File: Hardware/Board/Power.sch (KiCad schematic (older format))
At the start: 76 parts, among them Q1 Q_NMOS_DGS, Q2 Q_NMOS_DGS, Q3 Q_NMOS_DGS, Q4 Q_NMOS_DGS, U10 MAX17572, U11 MAX17572, U12 MAX17574, U8 MAX17572, U9 MAX17572

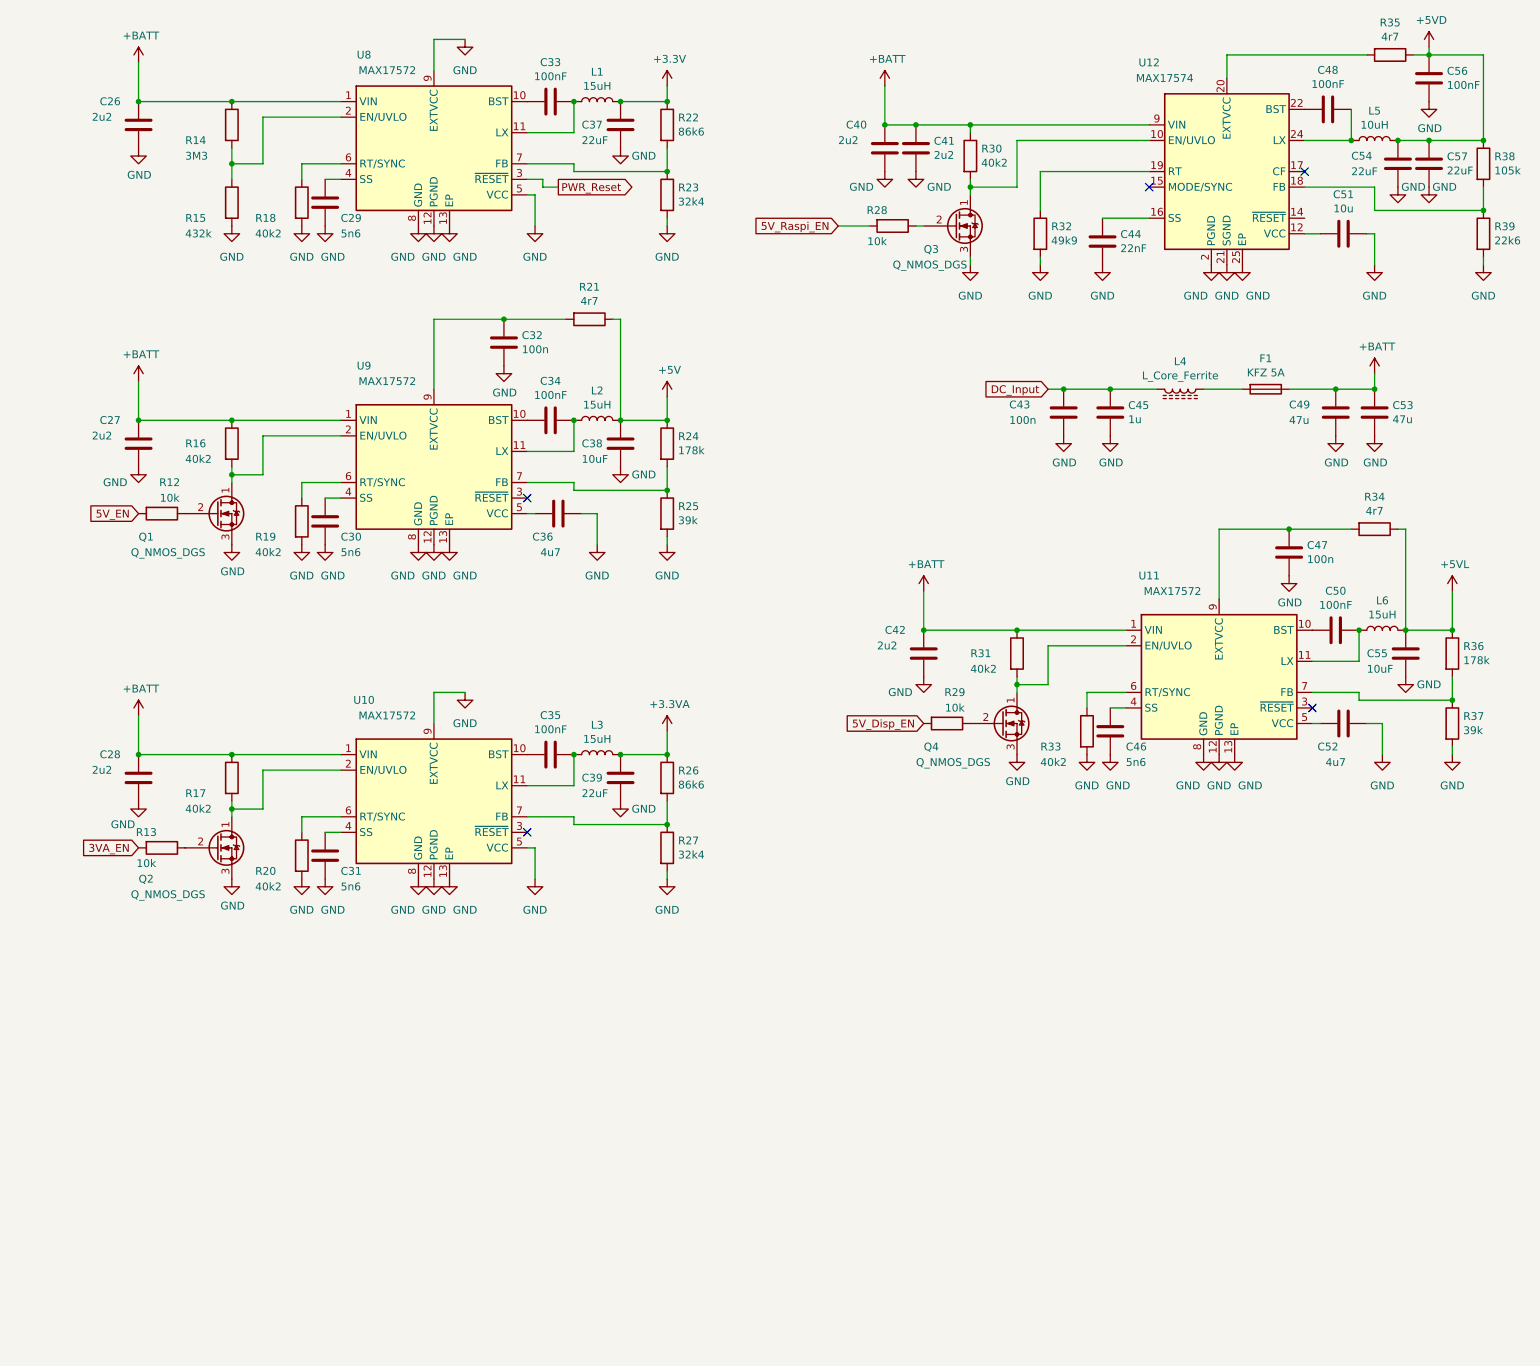
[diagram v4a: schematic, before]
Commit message: Octo SPI Flash und RAM zugefügt, weitere Bezeichnungen auf Stand gebracht
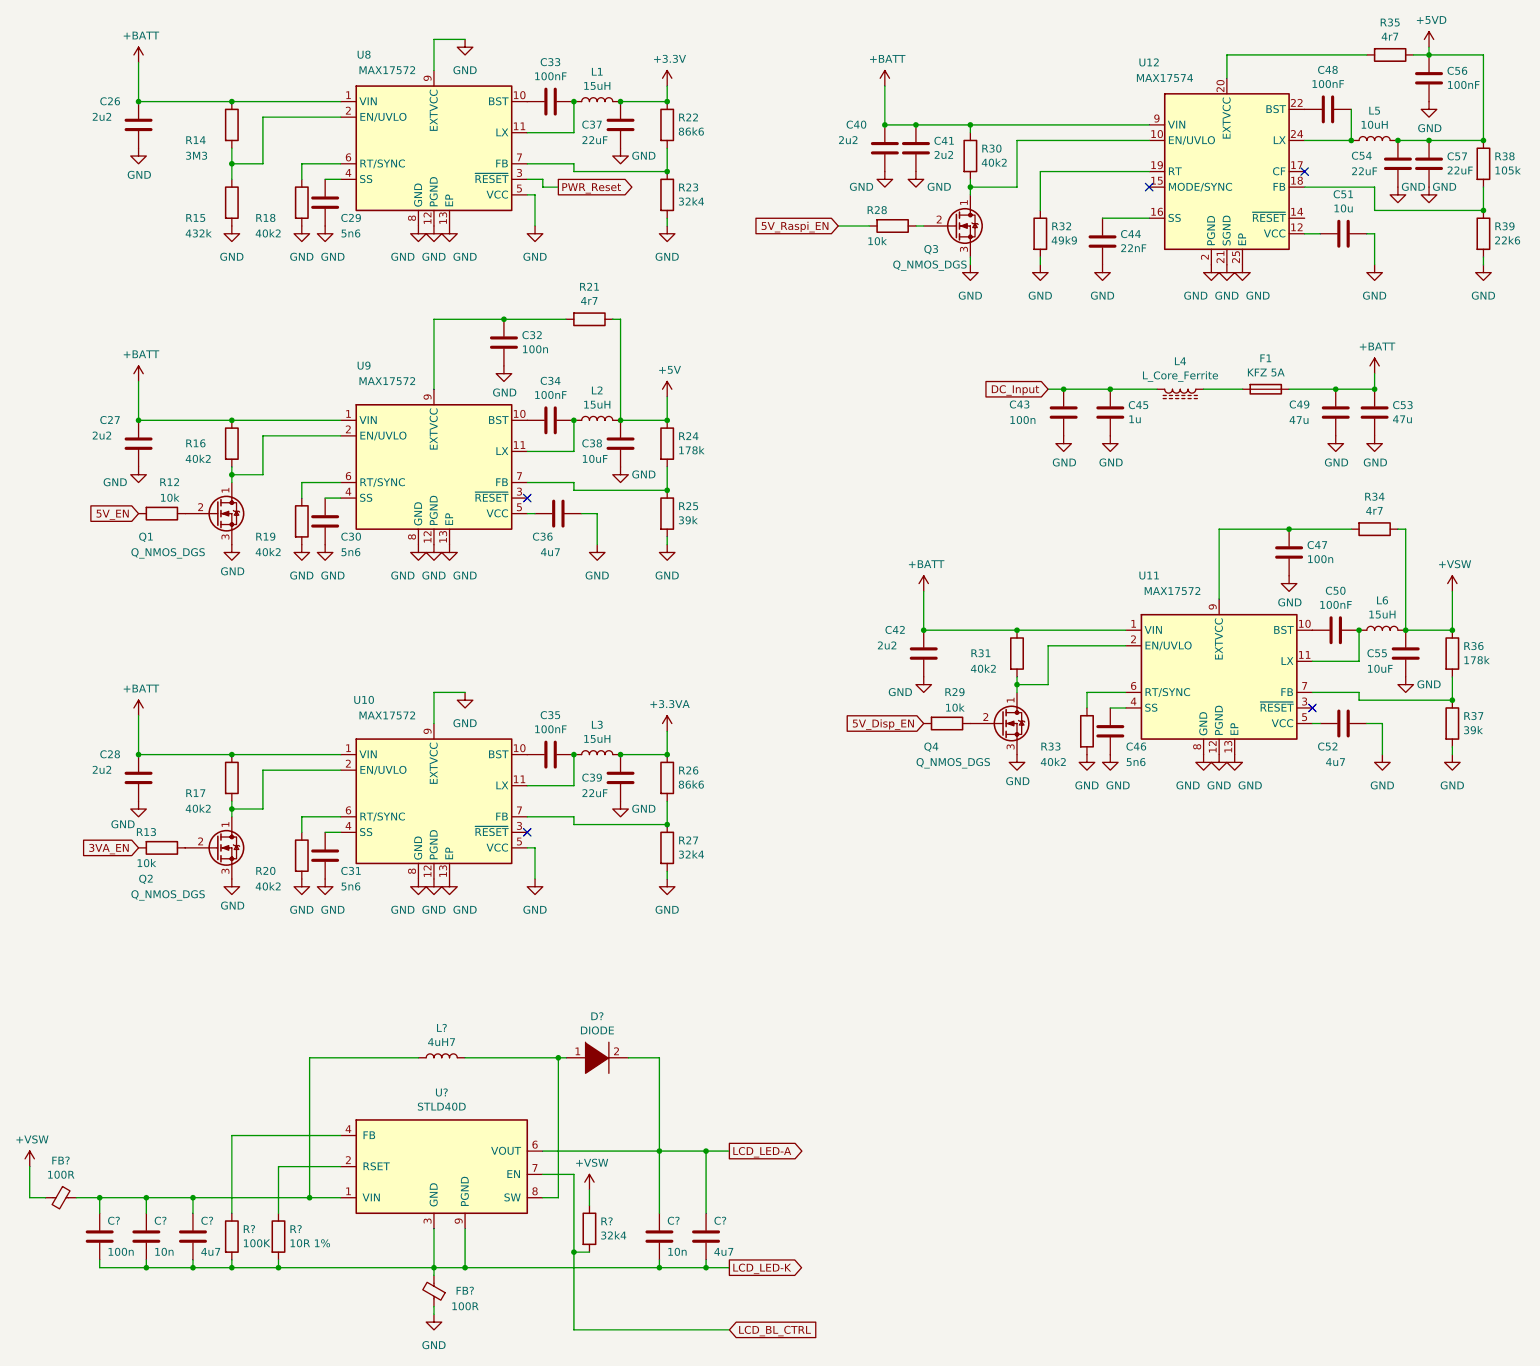
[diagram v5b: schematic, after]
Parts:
- added C? (x2): 4u7, Capacitor_SMD:C_0603_1608Metric, symbol Device:C
- added C? (x2): 10n, Capacitor_SMD:C_0603_1608Metric, symbol Device:C
- added C?: 100n, Capacitor_SMD:C_0603_1608Metric, symbol Device:C
- added D?: DIODE, symbol pspice:DIODE
- added FB? (x2): 100R, Inductor_SMD:L_0603_1608Metric, symbol Device:Ferrite_Bead_Small
- added L?: 4uH7, symbol Device:L
- added R?: 10R 1%, Resistor_SMD:R_0603_1608Metric, symbol Device:R
- added R?: 100K, Resistor_SMD:R_0603_1608Metric, symbol Device:R
- added R?: 32k4, Resistor_SMD:R_0603_1608Metric, symbol Device:R
- added U?: STLD40D, symbol DC_DC_Wandler:STLD40D
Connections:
- net GND: now also FB?.1
- net +5VL renamed +VSW
- net +VSW: now also FB?.2, R?.1
- new net: C?.1, C?.1, C?.1, FB?.1, L?.1, U?.1 (VIN)
- new net: R?.1, U?.2 (RSET)
- new net: R?.1, U?.4 (FB)
- new net: D?.1 (K), L?.2, U?.8 (SW)
- new net LCD_BL_CTRL: R?.2, U?.7 (EN)
- new net LCD_LED-A: C?.1, C?.1, D?.2 (A), U?.6 (VOUT)
- new net LCD_LED-K: C?.2, C?.2, C?.2, C?.2, C?.2, FB?.2, R?.2, R?.2, U?.3 (GND), U?.9 (PGND)

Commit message: Eine Menge Arbeit auf der GPN, fast fertig im Schaltplan.
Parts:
- removed Q4: Q_NMOS_DGS, symbol Device:Q_NMOS_DGS
- added Q?: Q_NMOS_DGS, symbol Device:Q_NMOS_DGS
- U?: symbol DC_DC_Wandler:STLD40D -> Womo-rescue:STLD40D-DC_DC_Wandler
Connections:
- net GND: now also Q?.3 (S)
- net at R31.2, U11.2 (EN/UVLO): now also Q?.1 (D)
- net at R29.1: now also Q?.2 (G)
- net 5V_Disp_EN renamed VSW_Disp_EN

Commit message: Board to Board Verbindung eingefügt
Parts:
- gave numbers to parts that had none: 14
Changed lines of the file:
@@
 EESchema Schematic File Version 4
 LIBS:Womo-cache
-EELAYER 29 0
+EELAYER 26 0
 EELAYER END
 $Descr A3 16535 11693
@@
 	10150 4750 10150 5000
 $Comp
-L Womo-rescue:STLD40D-DC_DC_Wandler U?
+L Womo-rescue:STLD40D-DC_DC_Wandler U16
 U 1 1 5DD49EC0
 P 3650 8050
-AR Path="/5C8BBC9A/5DD49EC0" Ref="U?"  Part="1"
+AR Path="/5C8BBC9A/5DD49EC0" Ref="U16"  Part="1"
 AR Path="/5E0C5EEA/5DD49EC0" Ref="U?"  Part="1"
-F 0 "U?" H 3650 8125 50  0000 C CNN
+F 0 "U16" H 3650 8125 50  0000 C CNN
 F 1 "STLD40D" H 3650 8034 50  0000 C CNN
 F 2 "" H 3650 8050 50  0001 C CNN
@@
 $EndComp
 $Comp
-L power:GND #PWR?
+L power:GND #PWR0228
 U 1 1 5DD5B9F7
 P 3600 9400
-AR Path="/5C8BBC9A/5DD5B9F7" Ref="#PWR?"  Part="1"
+AR Path="/5C8BBC9A/5DD5B9F7" Ref="#PWR0228"  Part="1"
 AR Path="/5E0C5EEA/5DD5B9F7" Ref="#PWR?"  Part="1"
-F 0 "#PWR?" H 3600 9150 50  0001 C CNN
+F 0 "#PWR0228" H 3600 9150 50  0001 C CNN
 F 1 "GND" H 3600 9200 50  0000 C CNN
 F 2 "" H 3600 9400 50  0001 C CNN
@@
 	2300 8250 2300 8750
 $Comp
-L Device:L L?
+L Device:L L7
 U 1 1 5DD8E83C
 P 3650 7750
-AR Path="/5C8BBC9A/5DD8E83C" Ref="L?"  Part="1"
+AR Path="/5C8BBC9A/5DD8E83C" Ref="L7"  Part="1"
 AR Path="/5E0C5EEA/5DD8E83C" Ref="L?"  Part="1"
-F 0 "L?" V 3840 7750 50  0000 C CNN
+F 0 "L7" V 3840 7750 50  0000 C CNN
 F 1 "4uH7" V 3749 7750 50  0000 C CNN
 F 2 "" H 3650 7750 50  0001 C CNN
@@
 P 1200 8650
 AR Path="/5C8BBC97/5DD99356" Ref="FB?"  Part="1"
-AR Path="/5C8BBC9A/5DD99356" Ref="FB?"  Part="1"
+AR Path="/5C8BBC9A/5DD99356" Ref="FB16"  Part="1"
 AR Path="/5E0C5EEA/5DD99356" Ref="FB?"  Part="1"
-F 0 "FB?" V 963 8650 50  0000 C CNN
+F 0 "FB16" V 963 8650 50  0000 C CNN
 F 1 "100R" V 1054 8650 50  0000 C CNN
 F 2 "Inductor_SMD:L_0603_1608Metric" V 1130 8650 50  0001 C CNN
@@
 $EndComp
 $Comp
-L Device:C C?
+L Device:C C69
 U 1 1 5DDA036C
 P 5350 8900
-AR Path="/5C8BBC9A/5DDA036C" Ref="C?"  Part="1"
+AR Path="/5C8BBC9A/5DDA036C" Ref="C69"  Part="1"
 AR Path="/5E0C5EEA/5DDA036C" Ref="C?"  Part="1"
-F 0 "C?" H 5400 9000 50  0000 L CNN
+F 0 "C69" H 5400 9000 50  0000 L CNN
 F 1 "4u7" H 5400 8800 50  0000 L CNN
 F 2 "Capacitor_SMD:C_0603_1608Metric" H 5388 8750 50  0001 C CNN
@@
 $EndComp
 $Comp
-L Device:C C?
+L Device:C C68
 U 1 1 5DDAD26E
 P 5050 8900
-AR Path="/5C8BBC9A/5DDAD26E" Ref="C?"  Part="1"
+AR Path="/5C8BBC9A/5DDAD26E" Ref="C68"  Part="1"
 AR Path="/5E0C5EEA/5DDAD26E" Ref="C?"  Part="1"
-F 0 "C?" H 5100 9000 50  0000 L CNN
+F 0 "C68" H 5100 9000 50  0000 L CNN
 F 1 "10n" H 5100 8800 50  0000 L CNN
 F 2 "Capacitor_SMD:C_0603_1608Metric" H 5088 8750 50  0001 C CNN
@@
 $EndComp
 $Comp
-L Device:C C?
+L Device:C C65
 U 1 1 5DDB39B0
 P 1450 8900
-AR Path="/5C8BBC9A/5DDB39B0" Ref="C?"  Part="1"
+AR Path="/5C8BBC9A/5DDB39B0" Ref="C65"  Part="1"
 AR Path="/5E0C5EEA/5DDB39B0" Ref="C?"  Part="1"
-F 0 "C?" H 1500 9000 50  0000 L CNN
+F 0 "C65" H 1500 9000 50  0000 L CNN
 F 1 "100n" H 1500 8800 50  0000 L CNN
 F 2 "Capacitor_SMD:C_0603_1608Metric" H 1488 8750 50  0001 C CNN
@@
 	2300 9050 2300 9100
 $Comp
-L Device:R R?
+L Device:R R50
 U 1 1 5DD79468
 P 2300 8900
-AR Path="/5C8BBC9A/5DD79468" Ref="R?"  Part="1"
+AR Path="/5C8BBC9A/5DD79468" Ref="R50"  Part="1"
 AR Path="/5E0C5EEA/5DD79468" Ref="R?"  Part="1"
-F 0 "R?" H 2370 8946 50  0000 L CNN
+F 0 "R50" H 2370 8946 50  0000 L CNN
 F 1 "100K" H 2370 8855 50  0000 L CNN
 F 2 "Resistor_SMD:R_0603_1608Metric" V 2230 8900 50  0001 C CNN
@@
 	2600 9050 2600 9100
 $Comp
-L Device:R R?
+L Device:R R51
 U 1 1 5DD6772F
 P 2600 8900
-AR Path="/5C8BBC9A/5DD6772F" Ref="R?"  Part="1"
+AR Path="/5C8BBC9A/5DD6772F" Ref="R51"  Part="1"
 AR Path="/5E0C5EEA/5DD6772F" Ref="R?"  Part="1"
-F 0 "R?" H 2670 8946 50  0000 L CNN
+F 0 "R51" H 2670 8946 50  0000 L CNN
 F 1 "10R 1%" H 2670 8855 50  0000 L CNN
 F 2 "Resistor_SMD:R_0603_1608Metric" V 2530 8900 50  0001 C CNN
@@
 P 3600 9250
 AR Path="/5C8BBC97/5DE658F8" Ref="FB?"  Part="1"
-AR Path="/5C8BBC9A/5DE658F8" Ref="FB?"  Part="1"
+AR Path="/5C8BBC9A/5DE658F8" Ref="FB17"  Part="1"
 AR Path="/5E0C5EEA/5DE658F8" Ref="FB?"  Part="1"
-F 0 "FB?" H 3400 9250 50  0000 C CNN
+F 0 "FB17" H 3400 9250 50  0000 C CNN
 F 1 "100R" H 3400 9350 50  0000 C CNN
 F 2 "Inductor_SMD:L_0603_1608Metric" V 3530 9250 50  0001 C CNN
@@
 	4400 7750 3800 7750
 $Comp
-L pspice:DIODE D?
+L pspice:DIODE D1
 U 1 1 5DEA7497
 P 4650 7750
-AR Path="/5C8BBC9A/5DEA7497" Ref="D?"  Part="1"
+AR Path="/5C8BBC9A/5DEA7497" Ref="D1"  Part="1"
 AR Path="/5E0C5EEA/5DEA7497" Ref="D?"  Part="1"
-F 0 "D?" H 4650 8015 50  0000 C CNN
+F 0 "D1" H 4650 8015 50  0000 C CNN
 F 1 "DIODE" H 4650 7924 50  0000 C CNN
 F 2 "" H 4650 7750 50  0001 C CNN
@@
 	5050 7750 5050 8350
 $Comp
-L Device:C C?
+L Device:C C67
 U 1 1 5DECFF34
 P 2050 8900
-AR Path="/5C8BBC9A/5DECFF34" Ref="C?"  Part="1"
+AR Path="/5C8BBC9A/5DECFF34" Ref="C67"  Part="1"
 AR Path="/5E0C5EEA/5DECFF34" Ref="C?"  Part="1"
-F 0 "C?" H 2100 9000 50  0000 L CNN
+F 0 "C67" H 2100 9000 50  0000 L CNN
 F 1 "4u7" H 2100 8800 50  0000 L CNN
 F 2 "Capacitor_SMD:C_0603_1608Metric" H 2088 8750 50  0001 C CNN
@@
 $EndComp
 $Comp
-L Device:C C?
+L Device:C C66
 U 1 1 5DECFF3B
 P 1750 8900
-AR Path="/5C8BBC9A/5DECFF3B" Ref="C?"  Part="1"
+AR Path="/5C8BBC9A/5DECFF3B" Ref="C66"  Part="1"
 AR Path="/5E0C5EEA/5DECFF3B" Ref="C?"  Part="1"
-F 0 "C?" H 1800 9000 50  0000 L CNN
+F 0 "C66" H 1800 9000 50  0000 L CNN
 F 1 "10n" H 1800 8800 50  0000 L CNN
 F 2 "Capacitor_SMD:C_0603_1608Metric" H 1788 8750 50  0001 C CNN
@@
 $EndComp
 $Comp
-L power:+VSW #PWR?
+L power:+VSW #PWR0248
 U 1 1 5DEDAB38
 P 10150 4750
-AR Path="/5C8BBC9A/5DEDAB38" Ref="#PWR?"  Part="1"
+AR Path="/5C8BBC9A/5DEDAB38" Ref="#PWR0248"  Part="1"
 AR Path="/5E0C5EEA/5DEDAB38" Ref="#PWR?"  Part="1"
-F 0 "#PWR?" H 10150 4600 50  0001 C CNN
+F 0 "#PWR0248" H 10150 4600 50  0001 C CNN
 F 1 "+VSW" H 10165 4923 50  0000 C CNN
 F 2 "" H 10150 4750 50  0001 C CNN
@@
 $EndComp
 $Comp
-L power:+VSW #PWR?
+L power:+VSW #PWR0251
 U 1 1 5DEDB132
 P 1000 8450
-AR Path="/5C8BBC9A/5DEDB132" Ref="#PWR?"  Part="1"
+AR Path="/5C8BBC9A/5DEDB132" Ref="#PWR0251"  Part="1"
 AR Path="/5E0C5EEA/5DEDB132" Ref="#PWR?"  Part="1"
-F 0 "#PWR?" H 1000 8300 50  0001 C CNN
+F 0 "#PWR0251" H 1000 8300 50  0001 C CNN
 F 1 "+VSW" H 1015 8623 50  0000 C CNN
 F 2 "" H 1000 8450 50  0001 C CNN
@@
 $EndComp
 $Comp
-L power:+VSW #PWR?
+L power:+VSW #PWR0252
 U 1 1 5DEDB25C
 P 4600 8600
-AR Path="/5C8BBC9A/5DEDB25C" Ref="#PWR?"  Part="1"
+AR Path="/5C8BBC9A/5DEDB25C" Ref="#PWR0252"  Part="1"
 AR Path="/5E0C5EEA/5DEDB25C" Ref="#PWR?"  Part="1"
-F 0 "#PWR?" H 4600 8450 50  0001 C CNN
+F 0 "#PWR0252" H 4600 8450 50  0001 C CNN
 F 1 "+VSW" H 4615 8773 50  0000 C CNN
 F 2 "" H 4600 8600 50  0001 C CNN
@@
 Connection ~ 5350 9100
 $Comp
-L Device:R R?
+L Device:R R52
 U 1 1 5DF3FE47
 P 4600 8850
-AR Path="/5C8BBC9A/5DF3FE47" Ref="R?"  Part="1"
+AR Path="/5C8BBC9A/5DF3FE47" Ref="R52"  Part="1"
 AR Path="/5E0C5EEA/5DF3FE47" Ref="R?"  Part="1"
-F 0 "R?" H 4670 8896 50  0000 L CNN
+F 0 "R52" H 4670 8896 50  0000 L CNN
 F 1 "32k4" H 4670 8805 50  0000 L CNN
 F 2 "Resistor_SMD:R_0603_1608Metric" V 4530 8850 50  0001 C CNN
@@
 	7350 5350 7350 5400
 $Comp
-L Device:Q_NMOS_DGS Q?
+L Device:Q_NMOS_DGS Q4
 U 1 1 5D1E6DA4
 P 7250 5600
-AR Path="/5C8BBC9A/5D1E6DA4" Ref="Q?"  Part="1"
+AR Path="/5C8BBC9A/5D1E6DA4" Ref="Q4"  Part="1"
 AR Path="/5E0C5EEA/5D1E6DA4" Ref="Q?"  Part="1"
-F 0 "Q?" H 7050 5450 50  0000 L CNN
+F 0 "Q4" H 7050 5450 50  0000 L CNN
 F 1 "Q_NMOS_DGS" H 6700 5350 50  0000 L CNN
 F 2 "" H 7450 5700 50  0001 C CNN
